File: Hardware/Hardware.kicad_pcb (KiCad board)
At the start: 2 copper layers, 42 x 14.5 mm, 40 parts, among them Y1 8MHz

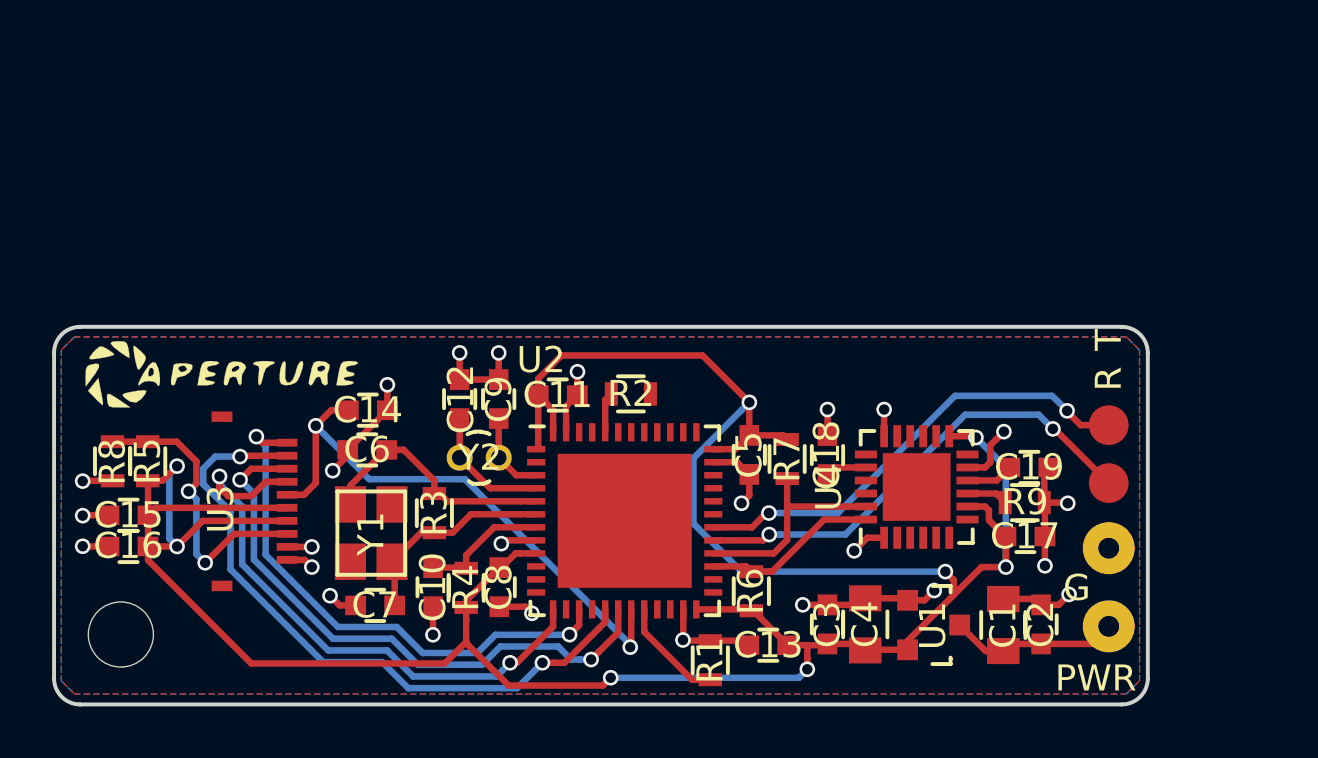
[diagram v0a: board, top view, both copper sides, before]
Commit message: feat: (4 Layer)
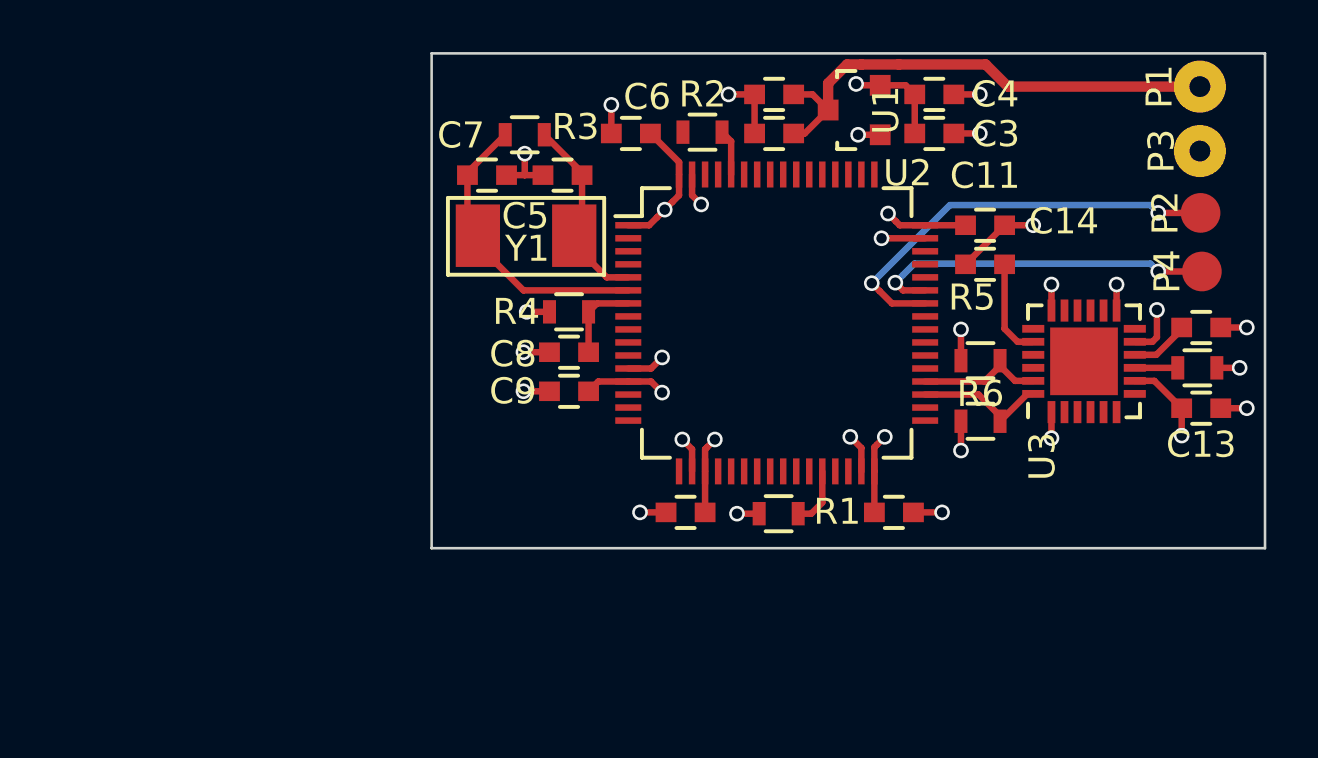
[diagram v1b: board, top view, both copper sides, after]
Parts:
- removed the ? at (185.0, 91.3)
- removed the ? at (185.0, 93.5)
- removed the ? at (150.9, 89.4)
- removed the ? at (147.1, 99.3)
- removed C16: 105, Capacitors_SMD:C_0603
- removed C17, C19: 104, Capacitors_SMD:C_0603
- removed C18: 2200pF, Capacitors_SMD:C_0603
- removed G, PWR: , Wire_Pads:SolderWirePad_single_0-8mmDrill
- removed R8: 0, Resistors_SMD:R_0603
- removed R9: 4.7K, Resistors_SMD:R_0603
- removed U4: , Housings_DFN_QFN:QFN-24-1EP_4x4mm_Pitch0.5mm
- removed Y2: , Crystals:Crystal_Round_Vertical_2mm
- added ?: , Symbols:Aperture_LOGO_20mm, B.Cu at (171.6, 87.4)
- added P1: +, Wire_Pads:SolderWirePad_single_0-8mmDrill, F.Cu at (188.5, 78.3)
- added P2: TX, Measurement_Points:Measurement_Point_Round-SMD-Pad_Small, F.Cu at (188.5, 83.1)
- added P3: -, Wire_Pads:SolderWirePad_single_0-8mmDrill, F.Cu at (188.5, 80.8)
- added P4: RX, Measurement_Points:Measurement_Point_Round-SMD-Pad_Small, F.Cu at (188.6, 85.4)
- C1, C4: footprint Capacitors_SMD:C_0805 -> Capacitors_SMD:C_0603
- C12, C9: value 12pF -> 104
- C14: value 104 -> 2200pF
- C15: value 105 -> 104
- C5: value 104 -> 20pF
- C6: value 20pF -> 104
- R5: value 0 -> 4.7K
- U1: value (none) -> LDO
- U2: value (none) -> STM32F103RCT6; footprint Housings_DFN_QFN:QFN-48-1EP_7x7mm_Pitch0.5mm -> Housings_QFP:LQFP-64_10x10mm_Pitch0.5mm
- U3: value (none) -> MPU6050; footprint Connectors_Molex:AYF531 -> Housings_DFN_QFN:QFN-24-1EP_4x4mm_Pitch0.5mm
- Y1: footprint Crystals:crystal_FA238-TSX3225 -> Crystals:SMD-5032
- moved C15 41.8 mm to (188.6, 87.5), turned to 0 degrees
- moved R5 32.0 mm to (180.1, 91.1), turned to 180 degrees
- moved U3 31.1 mm to (184.1, 88.8), turned to 90 degrees
- moved C14 24.4 mm to (180.2, 85.1), turned to 180 degrees
- moved C2 22.8 mm to (172.2, 78.6), turned to 180 degrees
- moved C1 20.8 mm to (172.2, 80.1), turned to 180 degrees
- moved C4 20.5 mm to (178.3, 78.6), turned to 0 degrees
- moved U1 20.0 mm to (175.2, 79.2), turned to 90 degrees
- moved C3 19.3 mm to (178.3, 80.1), turned to 0 degrees
- moved C13 19.0 mm to (188.6, 90.6)
- moved C11 17.7 mm to (180.2, 83.6)
- moved C12 17.2 mm to (176.8, 94.6), turned to 0 degrees
- moved C7 17.1 mm to (161.1, 81.7), turned to 0 degrees
- moved R7 16.1 mm to (188.4, 89.1), turned to 0 degrees
- moved C6 15.8 mm to (166.7, 80.1)
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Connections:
- C10 pad 1: RESET -> 3V3
- C12 pad 1: OSC32_OUT -> 3V3
- C13 pad 1: 3V3 -> GND
- C13 pad 2: GND -> 3V3
- C14 pad 1: LCD_DISP -> Net-(C14-Pad1)
- C15 pad 1: 3V3 -> Net-(C15-Pad1)
- C5 pad 1: 3V3 -> OSCIN
- C6 pad 1: OSCIN -> 3V3
- C8 pad 1: 3V3 -> RESET
- C9 pad 1: OSC32_IN -> 3V3
- R2 pad 1: Net-(R2-Pad1) -> (no net)
- R5 pad 1: 3V3 -> IMU_SDA
- R5 pad 2: MODE -> 3V3
- R6 pad 1: IMU_SDA -> 3V3
- R6 pad 2: 3V3 -> IMU_SCL
- R7 pad 1: 3V3 -> Net-(R7-Pad1)
- R7 pad 2: IMU_SCL -> GND
- U2 pad 10: Net-(U2-Pad10) -> (no net)
- U2 pad 11: Net-(U2-Pad11) -> (no net)
- U2 pad 12: Net-(U2-Pad12) -> GND
- U2 pad 13: LCD_COM -> 3V3
- U2 pad 14: Net-(U2-Pad14) -> (no net)
- U2 pad 15: LCD_SCLK -> (no net)
- U2 pad 16: Net-(U2-Pad16) -> (no net)
- U2 pad 17: LCD_SI -> (no net)
- U2 pad 18: LCD_SCS -> GND
- U2 pad 19: LCD_DISP -> 3V3
- U2 pad 2: Net-(U2-Pad2) -> (no net)
- U2 pad 20: BOOT1 -> (no net)
- U2 pad 21: Net-(U2-Pad21) -> (no net)
- U2 pad 22: Net-(U2-Pad22) -> (no net)
- U2 pad 23: GND -> (no net)
- U2 pad 24: 3V3 -> (no net)
- U2 pad 25: Net-(U2-Pad25) -> (no net)
- U2 pad 26: Net-(U2-Pad26) -> (no net)
- U2 pad 27: IMU_SDA -> (no net)
- U2 pad 28: IMU_SCL -> BOOT1
- U2 pad 29: USART_RX -> (no net)
- U2 pad 3: OSC32_IN -> (no net)
- U2 pad 30: USART_TX -> (no net)
- U2 pad 31: Net-(U2-Pad31) -> GND
- U2 pad 32: Net-(U2-Pad32) -> 3V3
- U2 pad 33: Net-(U2-Pad33) -> (no net)
- U2 pad 34: Net-(U2-Pad34) -> (no net)
- U2 pad 35: GND -> IMU_SDA
- U2 pad 36: 3V3 -> IMU_SCL
- U2 pad 37: Net-(U2-Pad37) -> (no net)
- U2 pad 38: Net-(U2-Pad38) -> (no net)
- U2 pad 39: Net-(U2-Pad39) -> (no net)
- U2 pad 4: OSC32_OUT -> (no net)
- U2 pad 40: Net-(U2-Pad40) -> (no net)
- U2 pad 41: Net-(U2-Pad41) -> (no net)
- U2 pad 42: Net-(U2-Pad42) -> USART_TX
- U2 pad 43: Net-(U2-Pad43) -> USART_RX
- U2 pad 44: BOOT0 -> (no net)
- U2 pad 45: Net-(U2-Pad45) -> (no net)
- U2 pad 46: Net-(U2-Pad46) -> (no net)
- U2 pad 8: GND -> (no net)
- U2 pad 9: 3V3 -> (no net)
- U3 pad 1: LCD_SCLK -> GND
- U3 pad 10: GND -> Net-(C15-Pad1)
- U3 pad 2: LCD_SI -> (no net)
- U3 pad 3: LCD_SCS -> (no net)
- U3 pad 4: LCD_COM -> (no net)
- U3 pad 5: LCD_DISP -> (no net)
- U3 pad 6: 3V3 -> (no net)
- U3 pad 7: 3V3 -> (no net)
- U3 pad 8: MODE -> 3V3
- U3 pad 9: GND -> Net-(R7-Pad1)
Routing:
- net 3V3: track 112.4 -> 29.3 mm, vias 8 -> 11
- net LCD_SI: track 25.5 -> 0.00 mm, vias 2 -> 0
- net LCD_SCS: track 22.7 -> 0.00 mm, vias 2 -> 0
- net LCD_COM: track 22.3 -> 0.00 mm, vias 2 -> 0
- net LCD_DISP: track 22.1 -> 0.00 mm, vias 2 -> 0
- net LCD_SCLK: track 20.6 -> 0.00 mm, vias 2 -> 0
- net GND: track 45.6 -> 31.0 mm, vias 25 -> 23
- net +3V3: track 6.53 -> 19.2 mm
- net MODE: track 11.4 -> 0.00 mm, vias 2 -> 0
- net OSC32_OUT: track 4.92 -> 0.00 mm
- net USART_RX: track 18.3 -> 13.5 mm
- net Net-(C14-Pad1): track 0.00 -> 3.78 mm
- net IMU_SCL: track 8.43 -> 4.84 mm
- net OSCOUT: track 8.01 -> 11.5 mm
- net OSC32_IN: track 3.22 -> 0.00 mm
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- added copper zone on In2.Cu, net 3V3
- added copper zone on In1.Cu, net GND
- removed copper zone on B.Cu, net GND
- removed copper zone on F.Cu, net GND
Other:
- board size 42 x 14.5 mm -> 32 x 19 mm
- copper layers 2 -> 4
- net class PWR added: clearance 0.2, trace_width 0.5, via_dia 0.6, via_drill 0.4
- rule pad_to_mask_clearance: 0.2 -> 0

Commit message: doc: 4 layer PCB
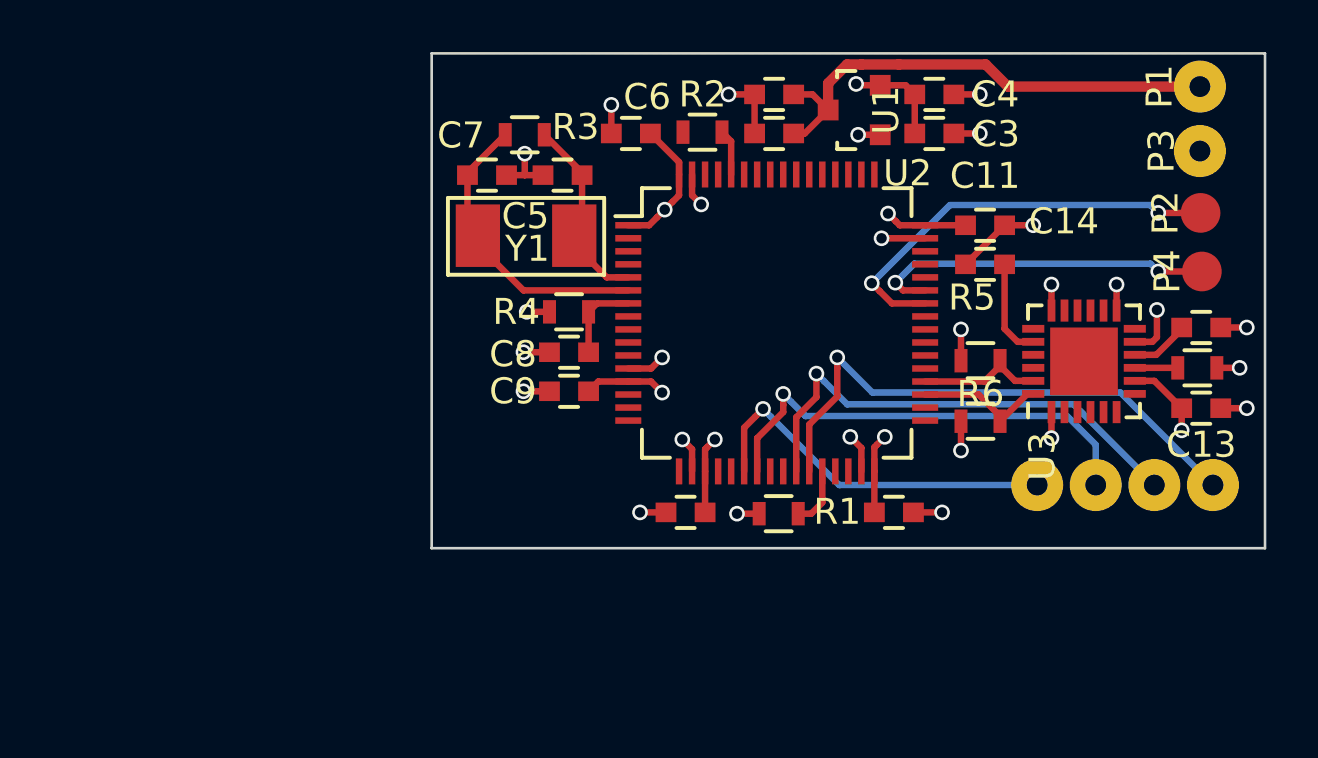
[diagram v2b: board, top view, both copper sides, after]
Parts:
- added P5: 1, Wire_Pads:SolderWirePad_single_0-8mmDrill, F.Cu at (182.2, 93.6)
- added P6: 2, Wire_Pads:SolderWirePad_single_0-8mmDrill, F.Cu at (184.5, 93.6)
- added P7: 3, Wire_Pads:SolderWirePad_single_0-8mmDrill, F.Cu at (186.8, 93.6)
- added P8: 4, Wire_Pads:SolderWirePad_single_0-8mmDrill, F.Cu at (189.0, 93.6)
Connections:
- U2 pad 22: (no net) -> BLDC1
- U2 pad 23: (no net) -> BLDC2
- U2 pad 26: (no net) -> BLDC3
- U2 pad 27: (no net) -> BLDC4
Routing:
- net BLDC4: track 0.00 -> 21.3 mm, vias 0 -> 1
- net BLDC3: track 0.00 -> 18.8 mm, vias 0 -> 1
- net BLDC2: track 0.00 -> 17.7 mm, vias 0 -> 1
- net BLDC1: track 0.00 -> 14.4 mm, vias 0 -> 1
- added copper zone on B.Cu, net GND
- added copper zone on F.Cu, net GND
